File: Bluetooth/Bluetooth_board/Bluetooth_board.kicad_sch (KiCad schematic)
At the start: 5 parts, among them J10 PINHD_1x2_Male, J11 PINHD_1x2_Male, J2 PINHD_1x6_Female, J6 PINHD_1x2_Male, U5 BM64SPKS1MC2-0003AA

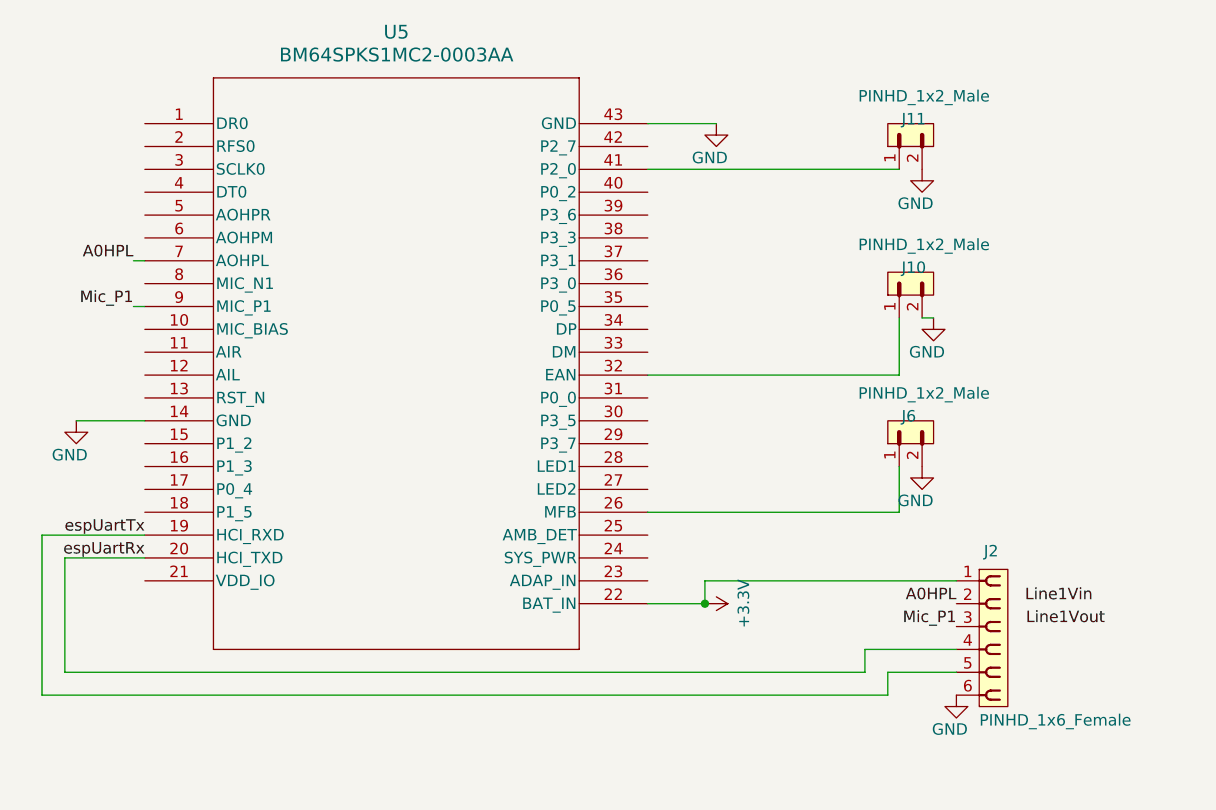
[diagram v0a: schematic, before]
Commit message: SMD5 + BM64 carrier: dedicated 3.3V rail, MFB pin, Vin protection, 8-pin link
Schematic work from the last few sessions' decisions:

SMD5 (Analog Redial 5)
- U5 XC6206P332MR (SOT-23) from +5V with C25/C26 1uF -> new +3V3_BM rail
  feeding the BM64 only, off the DevKit's own 3.3V
- BM64 header J12 -> J2, 6 -> 8 pins: +3V3_BM, AOHPL, MIC_P1, MIC_N1,
  U0RXD, U0TXD, MFB, GND
- MFB on GPIO15 with R17 100k pull-down (it's the BM64's power button --
  held from power-up it master-resets the pairing list)
- R16 1k in series into Line0Vin, and C23 10uF 0805 -> 1uF for the AOHPL
  coupling cap (Vin is 60k, not the few hundred ohms it was sized for)
- C24 1uF from MIC_N1 to GND (the differential mic input's AC ground)
- JP1 placed (Jumper_3_NC-1_Trace) for the planned MCLK/card-detect
  select, not wired yet

BM64 carrier board
- J2 -> J1, 8-pin socket mirroring the new SMD5 header, adding MIC_N1 and
  MFB
- New J2, 4-pin: P2_0 / RST_N / MFB, the one-time EEPROM-programming
  header that mates to J5 (replaces the loose J6/J10/J11 jumpers)

Co-Authored-By: Claude Opus 5 <noreply@anthropic.com>
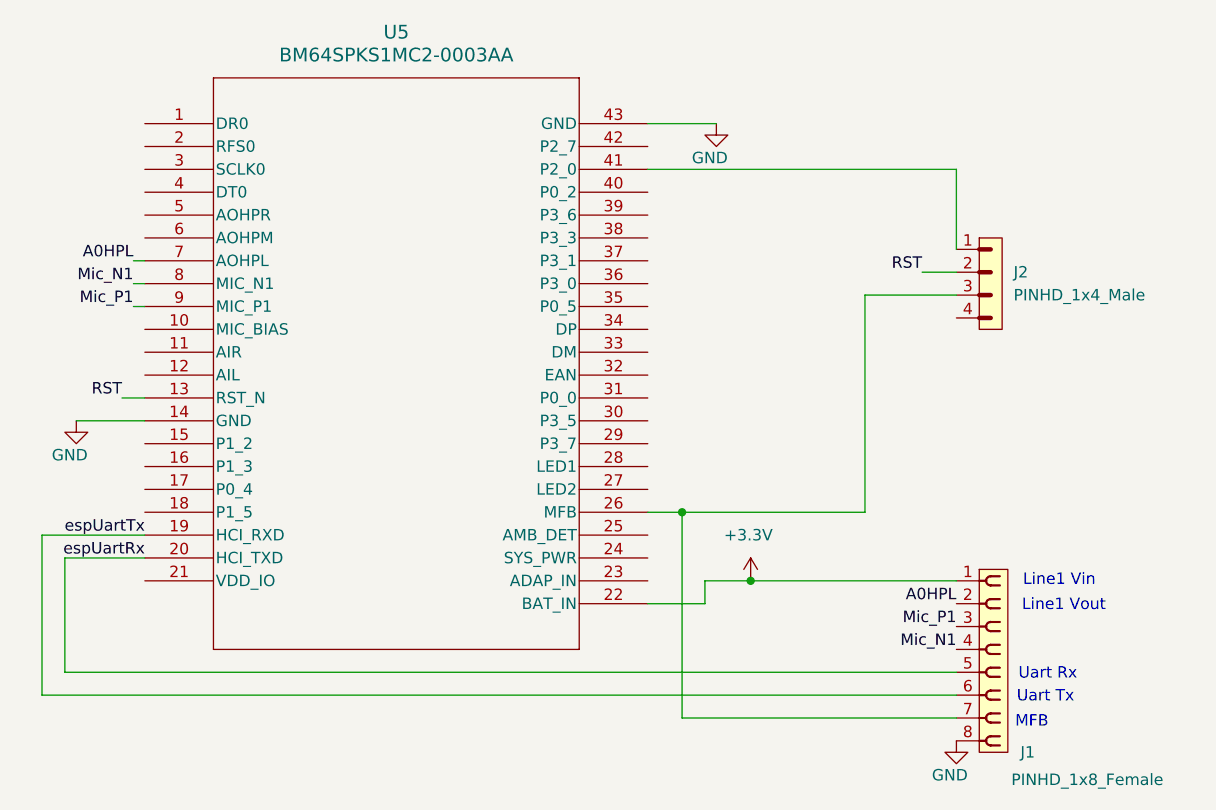
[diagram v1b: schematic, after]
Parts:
- removed J10, J11, J6: PINHD_1x2_Male, Connector_PinHeader_2.54mm:PinHeader_1x02_P2.54mm_Vertical, symbol PCM_SL_Pin_Headers:PINHD_1x2_Male
- removed J2: PINHD_1x6_Female, Connector_PinSocket_2.54mm:PinSocket_1x06_P2.54mm_Vertical, symbol PCM_SL_Pin_Headers:PINHD_1x6_Female
- added J1: PINHD_1x8_Female, Connector_PinSocket_2.54mm:PinSocket_1x08_P2.54mm_Vertical, symbol PCM_SL_Pin_Headers:PINHD_1x8_Female
- added J2: PINHD_1x4_Male, Connector_PinHeader_2.54mm:PinHeader_1x04_P2.54mm_Vertical, symbol PCM_SL_Pin_Headers:PINHD_1x4_Male
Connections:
- net +3.3V: now also J1.1
- net A0HPL: now also J1.2
- net GND: now also J1.8
- net Mic_P1: now also J1.3
- net espUartRx: now also J1.5
- net espUartTx: now also J1.6
- net at U5.26 (MFB): now also J1.7, J2.3
- net RST: now reaches U5.13 (RST_N)
- net RST: now also J2.2
- net at U5.41 (P2_0): now also J2.1
- net Mic_N1: now reaches U5.8 (MIC_N1)
- net Mic_N1: now also J1.4
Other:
- note added: "Line1 Vin"
- note added: "Line1 Vout"
- note added: "MFB"
- note added: "Uart Rx"
- note added: "Uart Tx"

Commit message: SMD5 + carrier: solder jumpers, C10/C11 to a disc footprint, 2-pin programming header
- SMD5: JP2/JP3 solder jumpers placed; C10/C11 100 uF 1206 -> 47 uF on
  Capacitor_THT:C_Disc_D4.7mm_W2.5mm_P5.00mm (DNP, fit 1 uF to use J7)
- Carrier: programming header down to 2 pins (P2_0, RST_N) now that MFB
  reaches the module through the main 8-pin link -- this also removes the
  hazard of MFB being driven from two connectors at once
- Cross-reference fixes missed by the hardware-doc split commit
- .gitignore: the Bluetooth carrier lives outside hardware/kicad/, so repeat
  the jlcpcb/, production_files/, tmp*.rpt and _restore_backup_* rules there

KNOWN ISSUE, not fixed here: carrier J1 pins 2 and 3 are swapped, so ESP TX
meets BM64 TX and ESP RX meets BM64 RX. See the next commit.

Co-Authored-By: Claude Opus 5 <noreply@anthropic.com>
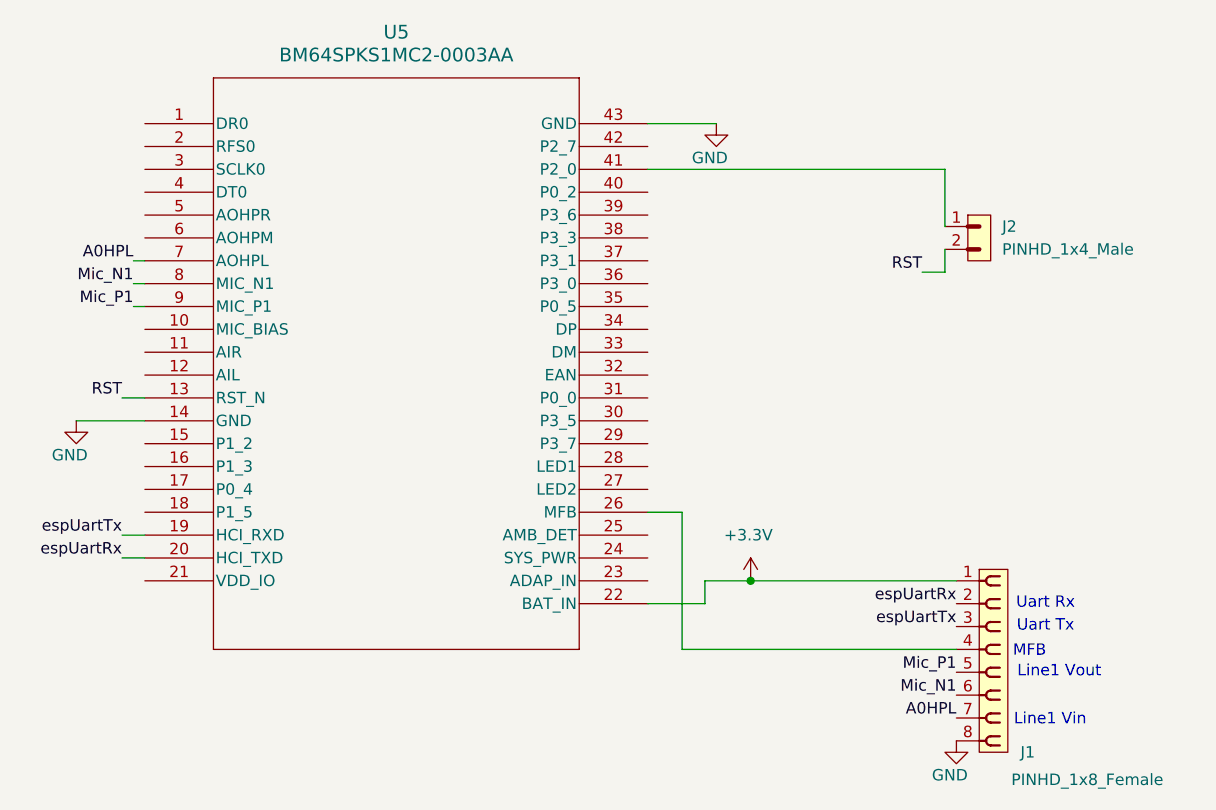
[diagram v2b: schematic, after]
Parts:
- J2: footprint Connector_PinHeader_2.54mm:PinHeader_1x04_P2.54mm_Vertical -> Connector_PinHeader_2.54mm:PinHeader_1x02_P2.54mm_Vertical; symbol PCM_SL_Pin_Headers:PINHD_1x4_Male -> PCM_SL_Pin_Headers:PINHD_1x2_Male
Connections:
- net A0HPL: now also J1.7; no longer J1.2
- net Mic_N1: now also J1.6; no longer J1.4
- net Mic_P1: now also J1.5; no longer J1.3
- net espUartRx: now also J1.2; no longer J1.5
- net espUartTx: now also J1.3; no longer J1.6
- new net: J1.4, U5.26 (MFB)
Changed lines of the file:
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@@
 	(text "Uart Tx"
 		(exclude_from_sim no)
-		(at 167.386 125.984 0)
+		(at 167.386 118.11 0)
 		(effects
 			(font
@@
 	(text "Line1 Vin"
 		(exclude_from_sim no)
-		(at 168.91 113.03 0)
+		(at 167.894 128.524 0)
 		(effects
 			(font
@@
 	(text "Uart Rx"
 		(exclude_from_sim no)
-		(at 167.64 123.444 0)
+		(at 167.386 115.57 0)
 		(effects
 			(font
@@
 	(text "Line1 Vout"
 		(exclude_from_sim no)
-		(at 169.418 115.824 0)
+		(at 168.91 123.19 0)
 		(effects
 			(font
@@
 	(text "MFB"
 		(exclude_from_sim no)
-		(at 165.862 128.778 0)
-		(effects
-			(font
-				(size 1.27 1.27)
-			)
-		)
-	)
-	(junction
-		(at 127 105.41)
-		(diameter 0)
-		(color 0 0 0 0)
+		(at 165.608 120.904 0)
+		(effects
+			(font
+				(size 1.27 1.27)
+			)
+		)
 	)
 	(junction
@@
 	(wire
 		(pts
-			(xy 55.88 107.95) (xy 55.88 125.73)
-		)
-		(stroke
-			(width 0)
-			(type default)
-		)
-	)
-	(wire
-		(pts
-			(xy 58.42 123.19) (xy 157.48 123.19)
-		)
-		(stroke
-			(width 0)
-			(type default)
-		)
-	)
-	(wire
-		(pts
-			(xy 67.31 110.49) (xy 58.42 110.49)
+			(xy 157.48 120.65) (xy 127 120.65)
+		)
+		(stroke
+			(width 0)
+			(type default)
+		)
+	)
+	(wire
+		(pts
+			(xy 156.21 67.31) (xy 156.21 73.66)
 		)
 		(stroke
@@
 	(wire
 		(pts
-			(xy 153.67 78.74) (xy 157.48 78.74)
-		)
-		(stroke
-			(width 0)
-			(type default)
-		)
-	)
-	(wire
-		(pts
 			(xy 66.04 80.01) (xy 67.31 80.01)
 		)
@@
 	(wire
 		(pts
-			(xy 55.88 125.73) (xy 157.48 125.73)
-		)
-		(stroke
-			(width 0)
-			(type default)
-		)
-	)
-	(wire
-		(pts
 			(xy 64.77 92.71) (xy 67.31 92.71)
 		)
@@
 	(wire
 		(pts
-			(xy 123.19 67.31) (xy 157.48 67.31)
-		)
-		(stroke
-			(width 0)
-			(type default)
-		)
-	)
-	(wire
-		(pts
-			(xy 58.42 110.49) (xy 58.42 123.19)
+			(xy 123.19 67.31) (xy 156.21 67.31)
+		)
+		(stroke
+			(width 0)
+			(type default)
+		)
+	)
+	(wire
+		(pts
+			(xy 156.21 78.74) (xy 156.21 76.2)
+		)
+		(stroke
+			(width 0)
+			(type default)
+		)
+	)
+	(wire
+		(pts
+			(xy 64.77 107.95) (xy 67.31 107.95)
 		)
 		(stroke
@@
 	(wire
 		(pts
+			(xy 153.67 78.74) (xy 156.21 78.74)
+		)
+		(stroke
+			(width 0)
+			(type default)
+		)
+	)
+	(wire
+		(pts
 			(xy 157.48 113.03) (xy 134.62 113.03)
 		)
@@
 	(wire
 		(pts
-			(xy 147.32 105.41) (xy 127 105.41)
-		)
-		(stroke
-			(width 0)
-			(type default)
-		)
-	)
-	(wire
-		(pts
-			(xy 157.48 81.28) (xy 147.32 81.28)
-		)
-		(stroke
-			(width 0)
-			(type default)
-		)
-	)
-	(wire
-		(pts
-			(xy 147.32 81.28) (xy 147.32 105.41)
+			(xy 64.77 110.49) (xy 67.31 110.49)
 		)
 		(stroke
@@
 	(wire
 		(pts
-			(xy 67.31 107.95) (xy 55.88 107.95)
-		)
-		(stroke
-			(width 0)
-			(type default)
-		)
-	)
-	(wire
-		(pts
 			(xy 129.54 113.03) (xy 129.54 115.57)
 		)
@@
 	(wire
 		(pts
-			(xy 157.48 128.27) (xy 127 128.27)
-		)
-		(stroke
-			(width 0)
-			(type default)
-		)
-	)
-	(wire
-		(pts
-			(xy 127 128.27) (xy 127 105.41)
-		)
-		(stroke
-			(width 0)
-			(type default)
-		)
-	)
-	(wire
-		(pts
-			(xy 157.48 67.31) (xy 157.48 76.2)
+			(xy 127 105.41) (xy 127 120.65)
 		)
 		(stroke
@@
 	)
 	(label "espUartTx"
-		(at 67.31 107.95 180)
+		(at 64.77 107.95 180)
 		(effects
 			(font
@@
 	)
 	(label "Mic_N1"
-		(at 157.48 120.65 180)
+		(at 157.48 125.73 180)
 		(effects
 			(font
@@
 	)
 	(label "espUartRx"
-		(at 67.31 110.49 180)
+		(at 64.77 110.49 180)
+		(effects
+			(font
+				(size 1.27 1.27)
+			)
+			(justify right bottom)
+		)
+	)
+	(label "espUartTx"
+		(at 157.48 118.11 180)
+		(effects
+			(font
+				(size 1.27 1.27)
+			)
+			(justify right bottom)
+		)
+	)
+	(label "espUartRx"
+		(at 157.48 115.57 180)
 		(effects
 			(font
@@
 	)
 	(label "A0HPL"
-		(at 157.48 115.57 180)
+		(at 157.48 128.27 180)
 		(effects
 			(font
@@
 	)
 	(label "Mic_P1"
-		(at 157.48 118.11 180)
+		(at 157.48 123.19 180)
 		(effects
 			(font
@@
 	)
 	(symbol
-		(lib_id "PCM_SL_Pin_Headers:PINHD_1x4_Male")
-		(at 161.29 80.01 0)
+		(lib_id "PCM_SL_Pin_Headers:PINHD_1x2_Male")
+		(at 160.02 74.93 0)
 		(unit 1)
 		(body_style 1)
@@
 		(fields_autoplaced yes)
 		(property "Reference" "J2"
-			(at 163.83 78.7399 0)
+			(at 162.56 73.6599 0)
 			(show_name no)
 			(do_not_autoplace no)
@@
 		)
 		(property "Value" "PINHD_1x4_Male"
-			(at 163.83 81.2799 0)
+			(at 162.56 76.1999 0)
 			(show_name no)
 			(do_not_autoplace no)
@@
 			)
 		)
-		(property "Footprint" "Connector_PinHeader_2.54mm:PinHeader_1x04_P2.54mm_Vertical"
-			(at 160.02 68.58 0)
+		(property "Footprint" "Connector_PinHeader_2.54mm:PinHeader_1x02_P2.54mm_Vertical"
+			(at 161.29 78.74 0)
 			(hide yes)
 			(show_name no)
@@
 		)
 		(property "Datasheet" ""
-			(at 161.29 69.85 0)
-			(hide yes)
-			(show_name no)
-			(do_not_autoplace no)
-			(effects
-				(font
-					(size 1.27 1.27)
-				)
-			)
-		)
-		(property "Description" "Pin Header male with pin space 2.54mm. Pin Count -4"
-			(at 161.29 80.01 0)
+			(at 160.02 67.31 0)
+			(hide yes)
+			(show_name no)
+			(do_not_autoplace no)
+			(effects
+				(font
+					(size 1.27 1.27)
+				)
+			)
+		)
+		(property "Description" "Pin Header male with pin space 2.54mm. Pin Count -2"
+			(at 160.02 74.93 0)
 			(hide yes)
 			(show_name no)
@@
 		(pin "1"
 		)
-		(pin "4"
-		)
-		(pin "3"
-		)
 		(instances
